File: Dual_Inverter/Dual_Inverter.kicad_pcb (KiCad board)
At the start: 2 copper layers, 15 x 10 mm, 10 parts, among them J1 CONN_01X04_MALE, J2 CONN_01X04_MALE, U1 MCP1754ST-3302E/MB-SOT-23, U2 NC7WZ14P6X

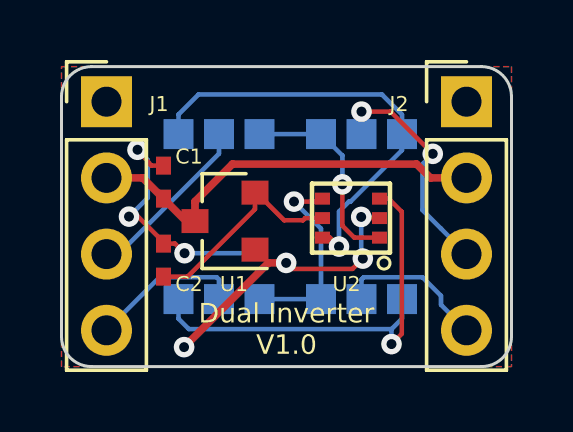
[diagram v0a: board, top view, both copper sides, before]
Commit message: Fixes a trace connection on the Dual Inverter and makes the solder jumper pads smaller.
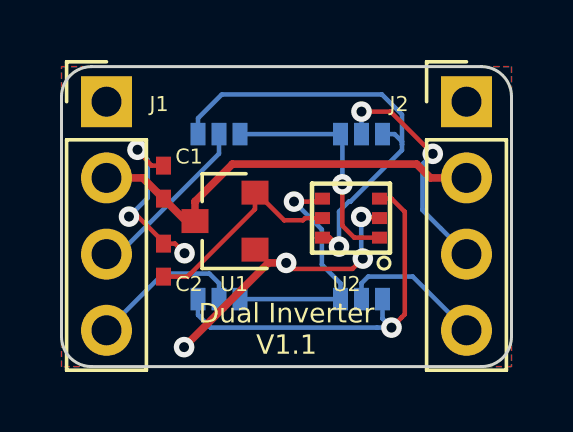
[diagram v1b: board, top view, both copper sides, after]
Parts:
- A1, A2, B1, B2: footprint jumper:SOLDER-JUMPER_2-WAY -> local:SOLDER-JUMPER_2-WAY
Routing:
- net GND: track 18.3 -> 16.1 mm
- net Net-(B1-Pad1): track 15.0 -> 13.3 mm
- net Net-(B1-Pad3): track 6.66 -> 8.23 mm
- net Net-(A1-Pad3): track 6.80 -> 7.83 mm
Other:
- board text added: "Dual Inverter V1.1"
- board text removed: "Dual Inverter V1.0"
